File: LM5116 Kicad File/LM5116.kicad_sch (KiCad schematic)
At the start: 84 parts, among them J1 XT60-M, J10 PH1-01-UA, J11 PH1-01-UA, J12 PH1-01-UA, J13 PH1-01-UA, J14 61300311121, J15 61300311121, J16 61300311121, J17 61300311121, J18 61300311121, J19 61300311121, J2 PH1-01-UA, J20 61300311121, J21 61300311121, J22 61300311121, J23 61300311121, J24 61300311121, J25 61300311121, J3 PH1-01-UA, J4 PH1-01-UA, J5 PH1-01-UA, J6 PH1-01-UA, J7 PH1-01-UA, J8 PH1-01-UA, J9 PH1-01-UA, Q1 CSD17304Q3, Q2 CSD17304Q3, Q3 CSD17304Q3, Q4 CSD17304Q3, Q5 2N7002, Q6 IQDH29NE2LM5CG, U1 LM25116MHX/NOPB, U2 TLV1701AIDBVR, U3 TL431DBZ

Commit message: New Kicad File Final
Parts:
- C4: value 100u -> 680u; footprint Capacitor_SMD:CP_Elec_6.3x5.8 -> Capacitor_SMD:CP_Elec_10x10.5
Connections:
- net 1: now also J14.1; no longer J14.2
- net 10: now also J22.1; no longer J22.2
- net 11: now also J21.1; no longer J21.2
- net 12: now also J20.1; no longer J20.2
- net 2: now also J15.1; no longer J15.2
- net 3: now also J16.1; no longer J16.2
- net 4: now also J17.1; no longer J17.2
- net 5: now also J18.1; no longer J18.2
- net 6: now also J19.1; no longer J19.2
- net 7: now also J25.1; no longer J25.2
- net 8: now also J24.1; no longer J24.2
- net 9: now also J23.1; no longer J23.2
- net VOUT: now also J14.2, J15.2, J16.2, J17.2, J18.2, J19.2, J20.2, J21.2, J22.2, J23.2, J24.2, J25.2; no longer J14.1, J15.1, J16.1, J17.1, J18.1, J19.1, J20.1, J21.1, J22.1, J23.1, J24.1, J25.1

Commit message: Update Kicad File
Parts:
- C2: value 220p -> 180p; footprint Capacitor_SMD:C_0603_1608Metric_Pad1.08x0.95mm_HandSolder -> Capacitor_SMD:C_0402_1005Metric_Pad0.74x0.62mm_HandSolder
- C3: value 100p -> 33n; footprint Capacitor_SMD:C_0201_0603Metric_Pad0.64x0.40mm_HandSolder -> Capacitor_SMD:C_0805_2012Metric_Pad1.18x1.45mm_HandSolder
- R2: value 10k -> 22.6k
- R3: value 1.5k -> 2.49k; footprint Resistor_SMD:R_0402_1005Metric_Pad0.72x0.64mm_HandSolder -> Resistor_SMD:R_0603_1608Metric_Pad0.98x0.95mm_HandSolder
- R5: value 10.2k -> 5.3k; footprint Resistor_SMD:R_0805_2012Metric_Pad1.20x1.40mm_HandSolder -> Resistor_SMD:R_0603_1608Metric_Pad0.98x0.95mm_HandSolder
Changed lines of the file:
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@@
 			)
 		)
-		(property "Value" "10.2k"
+		(property "Value" "5.3k"
 			(at 49.53 124.4599 0)
 			(show_name no)
@@
 			)
 		)
-		(property "Footprint" "Resistor_SMD:R_0805_2012Metric_Pad1.20x1.40mm_HandSolder"
+		(property "Footprint" "Resistor_SMD:R_0603_1608Metric_Pad0.98x0.95mm_HandSolder"
 			(at 48.006 123.444 90)
 			(hide yes)
@@
 			)
 		)
-		(property "Value" "100p"
+		(property "Value" "33n"
 			(at 92.71 48.26 90)
 			(show_name no)
@@
 			)
 		)
-		(property "Footprint" "Capacitor_SMD:C_0201_0603Metric_Pad0.64x0.40mm_HandSolder"
+		(property "Footprint" "Capacitor_SMD:C_0805_2012Metric_Pad1.18x1.45mm_HandSolder"
 			(at 92.71 41.91 0)
 			(hide yes)
@@
 			)
 		)
-		(property "Value" "220p"
+		(property "Value" "180p"
 			(at 92.456 31.75 90)
 			(show_name no)
@@
 			)
 		)
-		(property "Footprint" "Capacitor_SMD:C_0603_1608Metric_Pad1.08x0.95mm_HandSolder"
+		(property "Footprint" "Capacitor_SMD:C_0402_1005Metric_Pad0.74x0.62mm_HandSolder"
 			(at 92.71 36.83 0)
 			(hide yes)
@@
 			)
 		)
-		(property "Value" "1.5k"
+		(property "Value" "2.49k"
 			(at 58.42 92.7099 0)
 			(show_name no)
@@
 			)
 		)
-		(property "Footprint" "Resistor_SMD:R_0402_1005Metric_Pad0.72x0.64mm_HandSolder"
+		(property "Footprint" "Resistor_SMD:R_0603_1608Metric_Pad0.98x0.95mm_HandSolder"
 			(at 56.896 91.694 90)
 			(hide yes)
@@
 			)
 		)
-		(property "Value" "10k"
+		(property "Value" "22.6k"
 			(at 58.42 72.3899 0)
 			(show_name no)

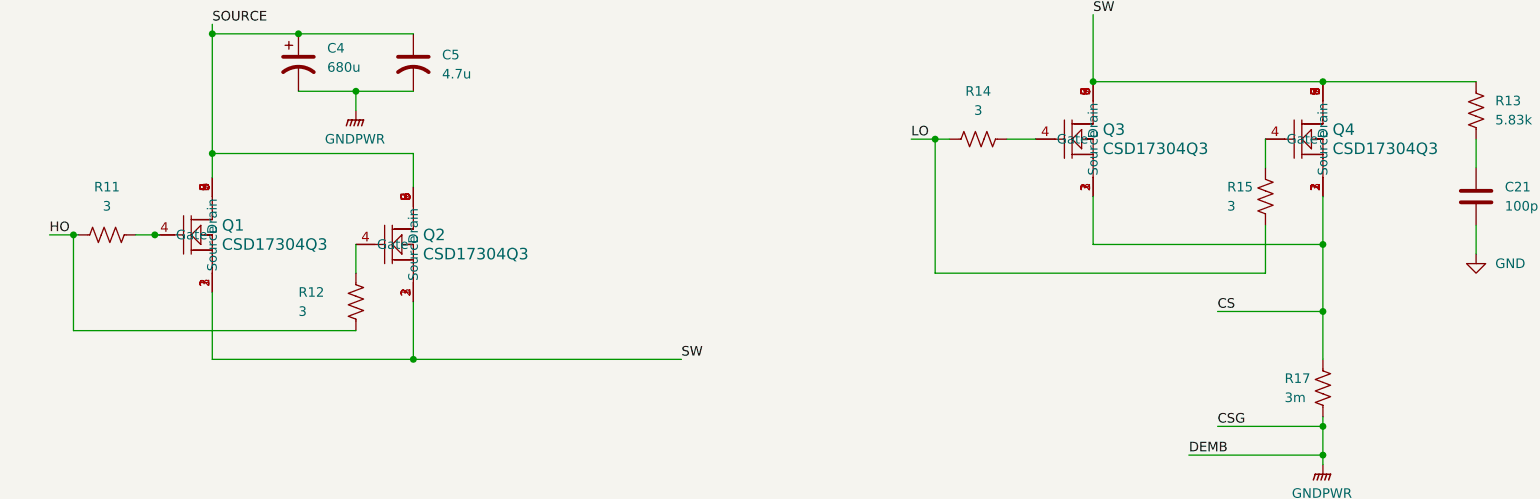
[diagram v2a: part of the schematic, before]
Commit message: Update Adding pulldown resistor
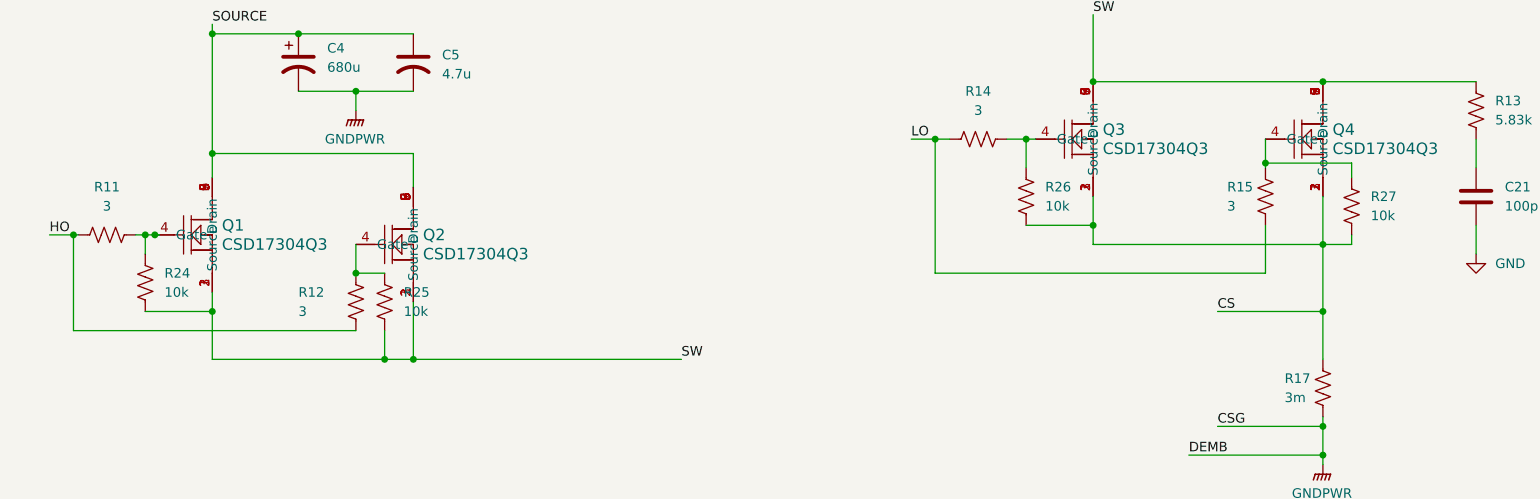
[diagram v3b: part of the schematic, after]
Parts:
- added R24, R25, R26, R27: 10k, Resistor_SMD:R_0402_1005Metric_Pad0.72x0.64mm_HandSolder, symbol Device:R_US
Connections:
- net CS: now also R26.1, R27.1
- net SW: now also R24.1, R25.1
- net at Q4.4 (Gate), R15.2: now also R27.2
- net at Q1.4 (Gate), R11.2: now also R24.2
- net at Q2.4 (Gate), R12.1: now also R25.2
- net at Q3.4 (Gate), R14.2: now also R26.2
